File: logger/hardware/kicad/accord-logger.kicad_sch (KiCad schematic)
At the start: 91 parts, among them J1 Power 2-way, J2 Cluster harness 8-way, J3 Bus / expansion (unpopulated), J4 Service 4-way, J5 SD breakout 6-way, Q1 IRF4905PbF, Q2 2N3904, Q3 2N3904, U1 RaspberryPi_Pico_W, U2 PC817, U3 LM2678T-5.0, X1 SIGNAL_ISOLATION (required), X2 SIGNAL_ISOLATION (under revie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, X3 SIGNAL_ISOLATION (under revie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, X4 SIGNAL_ISOLATION (under revie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, X5 SIGNAL_ISOLATION (under revie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, X6 IGN_QUALIFICATION, X7 VEHICLE_PROTECTION, X8 MAX_ON

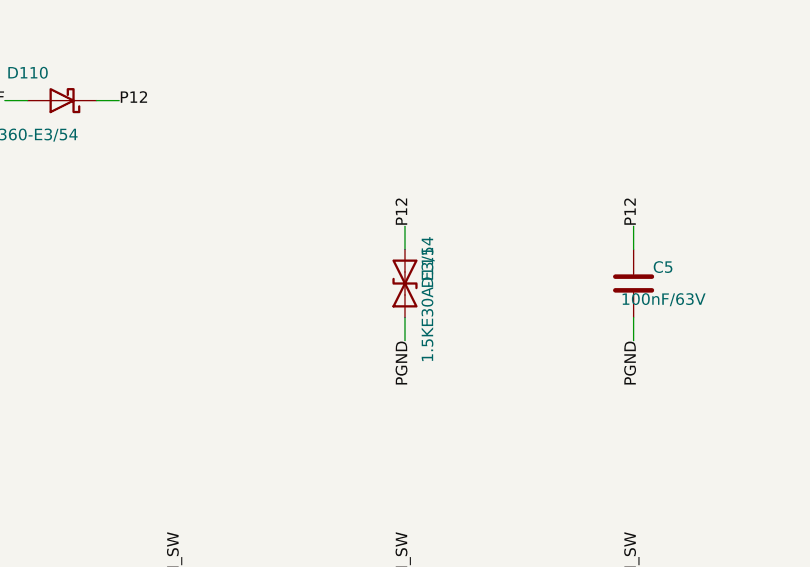
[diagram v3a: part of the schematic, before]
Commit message: logger-schematic: correct the reversed input TVS, and assert hidden polarity
Applies review finding R06-REV-4, blocking, from
coordination/reviews/LRA06_REVIEW_2026-10-29.md.

The input TVS was drawn backwards: D111 pin 1 on PGND and pin 2 on P12,
against DESIGN.md section 3, which puts the cathode on P12. The specified
Vishay 1.5KE30A-E3/54 is unidirectional, so built as drawn it is a
forward-biased rectifier across the supply: it conducts at about a volt and
shorts P12. Pin 1 now goes to P12 and pin 2 to PGND, and the symbol is
rotated so pin 1 sits at the top and the drawing reads correctly.

Verified before changing anything: the footprint puts pad 1 at x=0 with the
silkscreen band at x=2.9-3.1 mm, so pad 1 is the banded cathode end.

Why the existing checks did not catch it. Device:D_TVS names its pins A1 and
A2 because it is a bidirectional symbol: it draws no cathode bar and asserts
no polarity, so neither ERC nor a reader can see a reversal. The part's own
BOM note says to check the cathode net rather than trust the footprint, and
DESIGN.md section 3 records this exact part being fitted backwards once
before - and the capture still got it wrong, because the symbol had deleted
the thing the note tells you to check.

This is R06-REV-1's lesson in another costume, so the fix is the same shape.
A new CAPTURE_NOTES section 3 states the pin-to-net mapping for every part
whose symbol cannot carry it, since no symbol will tell the next reader:
the TVS, the three electrolytics where Device:C_Polarized leaves both pins
unnamed and pin 1 is positive, and the PC817 whose four pins are all
unnamed. All are now asserted by pin number in check_capture.py.

A guard fails if any future part arrives whose symbol cannot express
polarity and which carries no such assertion. It derives opacity from the
netlist itself - a part whose pins have no pinfunction, or only A1/A2 -
rather than from a hand-maintained list of symbols. Tested by removing the
TVS entry: it flags D111 on its 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
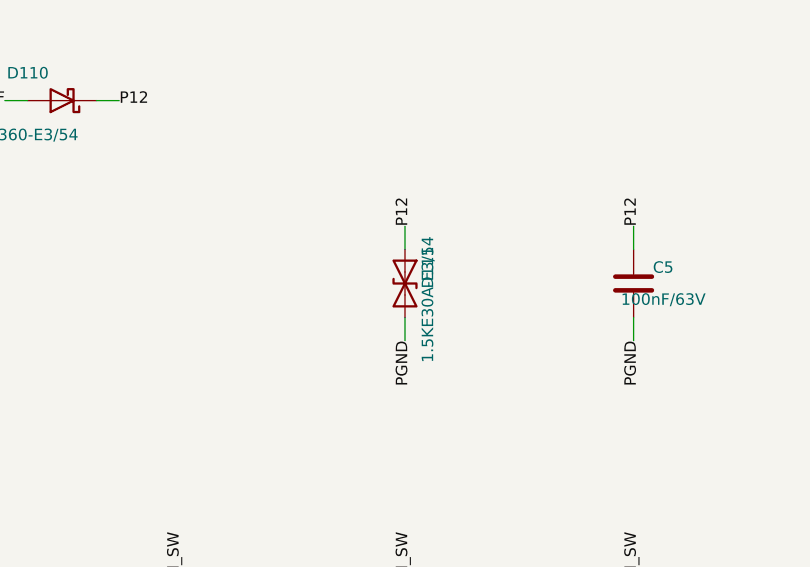
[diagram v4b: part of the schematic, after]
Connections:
- net P12: now also D111.1 (A1); no longer D111.2 (A2)
- net PGND: now also D111.2 (A2); no longer D111.1 (A1)
